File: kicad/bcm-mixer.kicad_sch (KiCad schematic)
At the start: 42 parts, among them J1 AudioJack2_SwitchT, J10 Conn_01x08_Pin, J11 Conn_01x08_Socket, J12 Conn_01x08_Socket, J13 Conn_01x08_Pin, J14 Conn_01x06_Pin, J15 Conn_01x06_Socket, J16 Conn_01x06_Socket, J17 Conn_01x06_Pin, J2 AudioJack2_SwitchT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

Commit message: Updating everything and adding gerbers
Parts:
- removed RV3, RV6: 100kA, Rumblesan_Potentiometer_THT:Potentiometer_TTElectronics_PS45_Dual_Frame, symbol Standard_Parts:R_Potentiometer
- added H1, H2, H3, H4: MountingHole_Pad, Rumblesan_Standard_Parts:MountingHole_3.2mm_M3_DIN965_Pad, symbol Mechanical:MountingHole_Pad
- added RV3, RV6: 100kA, Rumblesan_Potentiometer_THT:Potentiometer_TTElectronics_PS45_Dual_Frame, symbol Rumblesan_Standard_Parts:R_Potentiometer_Dual_Separate
- C19, C20: footprint Capacitor_THT:CP_Radial_D5.0mm_P2.00mm -> Rumblesan_Standard_Parts:CP_Radial_D5.0mm_P2.00mm; symbol Standard_Parts:C_Polarized -> Rumblesan_Standard_Parts:C_Polarized
- R10, R11, R12, R13, R16, R17, R24, R25, R31, R32, R35, R36, R40, R41: symbol Standard_Parts:R -> Rumblesan_Standard_Parts:R
- RV1, RV4: symbol Standard_Parts:R_Potentiometer_Dual_Separate -> Rumblesan_Standard_Parts:R_Potentiometer_Dual_Separate
- RV10, RV2, RV5, RV9: symbol Standard_Parts:R_Potentiometer -> Rumblesan_Standard_Parts:R_Potentiometer
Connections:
- net CHAN1_LEVEL_CENTER_CTRL: now also RV3.2
- net CHAN1_LEVEL_CW_CTRL: now also RV3.3
- net CHAN1_PAN_CCW_MAIN: now also R11.2, R13.1; no longer R11.1, R13.2
- net CHAN1_PAN_CW_MAIN: now also R10.2, R12.1; no longer R10.1, R12.2
- net CHAN2_LEVEL_CENTER_CTRL: now also RV6.2
- net CHAN2_LEVEL_CW_CTRL: now also RV6.3
- net CHAN2_PAN_CCW_MAIN: now also R17.2, R24.1; no longer R17.1, R24.2
- net CHAN2_PAN_CW_MAIN: now also R16.2, R25.1; no longer R16.1, R25.2
- net GND: now also H1.1, H2.1, H3.1, H4.1, RV3.1, RV3.6, RV6.1, RV6.6
- net L_OUT_MAIN: now also R40.2; no longer R40.1
- net MAIN_BUS_L: now also R12.2, R25.2, R31.2, R35.2; no longer R12.1, R25.1, R31.1, R35.1
- net MAIN_BUS_R: now also R13.2, R24.2, R32.2, R36.1; no longer R13.1, R24.1, R32.1, R36.2
- net Main Channel/L_OUT: now also R40.1; no longer R40.2
- net Main Channel/R_OUT: now also R41.1; no longer R41.2
- net Mono Channel 1/OUTPUT: now also R10.1, R11.1; no longer R10.2, R11.2
- net Mono Channel 2/OUTPUT: now also R16.1, R17.1; no longer R16.2, R17.2
- net R_OUT_MAIN: now also R41.2; no longer R41.1
- net at J14.3 (Pin_3): now also R32.1; no longer R32.2
- net at J14.5 (Pin_5): now also R31.1; no longer R31.2
- net at J8.7 (Pin_7), J8.8 (Pin_8): now also R36.2; no longer R36.1
- net at J8.3 (Pin_3), J8.4 (Pin_4): now also R35.1; no longer R35.2
- no-connect marks 4 -> 8

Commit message: Updating power header symbol
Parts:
- J6: footprint Rumblesan_Eurorack_Power:Eurorack_PowerHeader_2x05_P2.54mm_Shrouded -> Rumblesan_Eurorack_Power:Eurorack_Power_IDC-Header_2x05_P2.54mm_Vertical

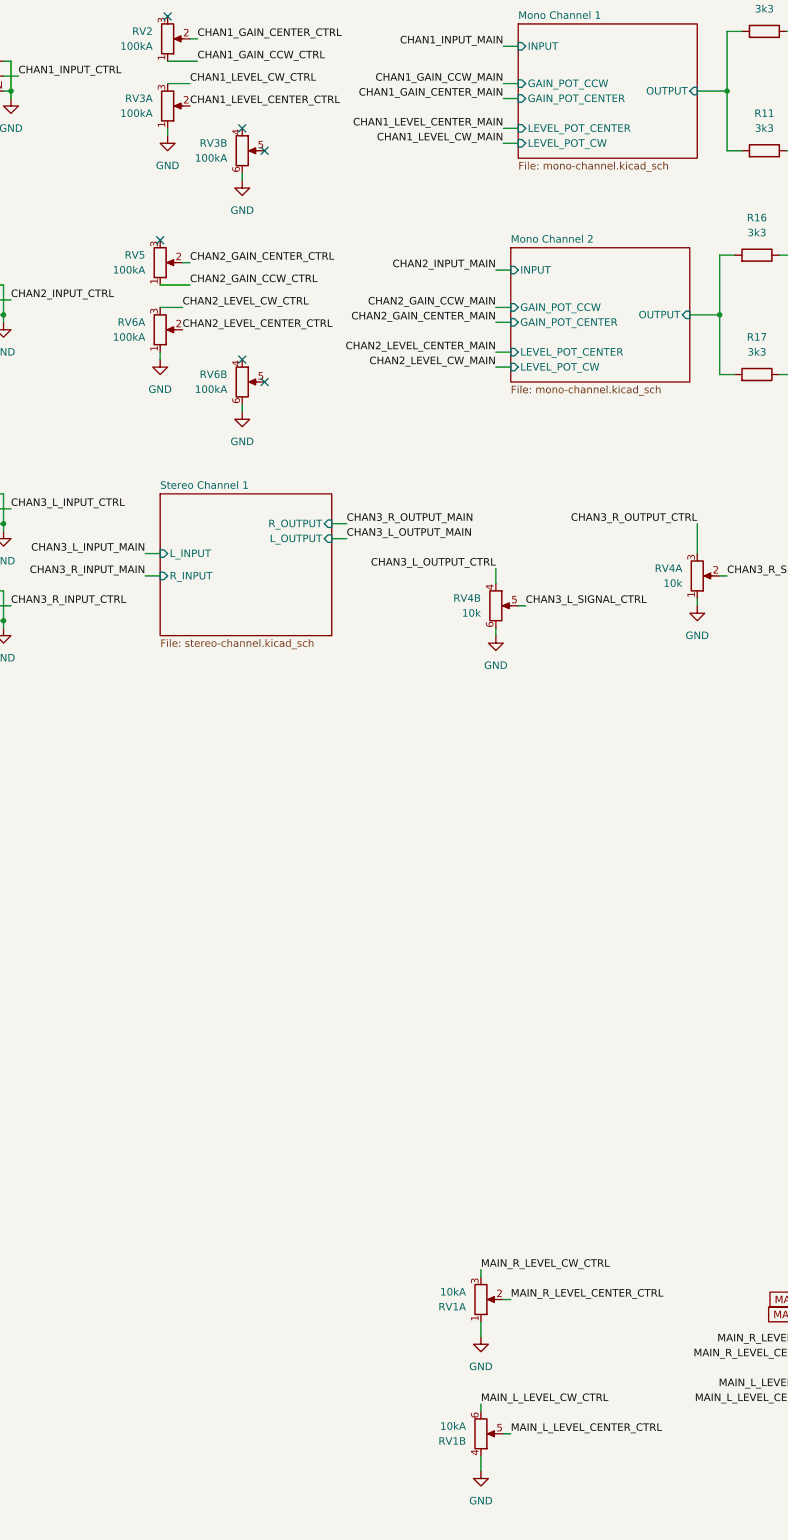
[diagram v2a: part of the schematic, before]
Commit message: Update slide pot values based on what's actually available
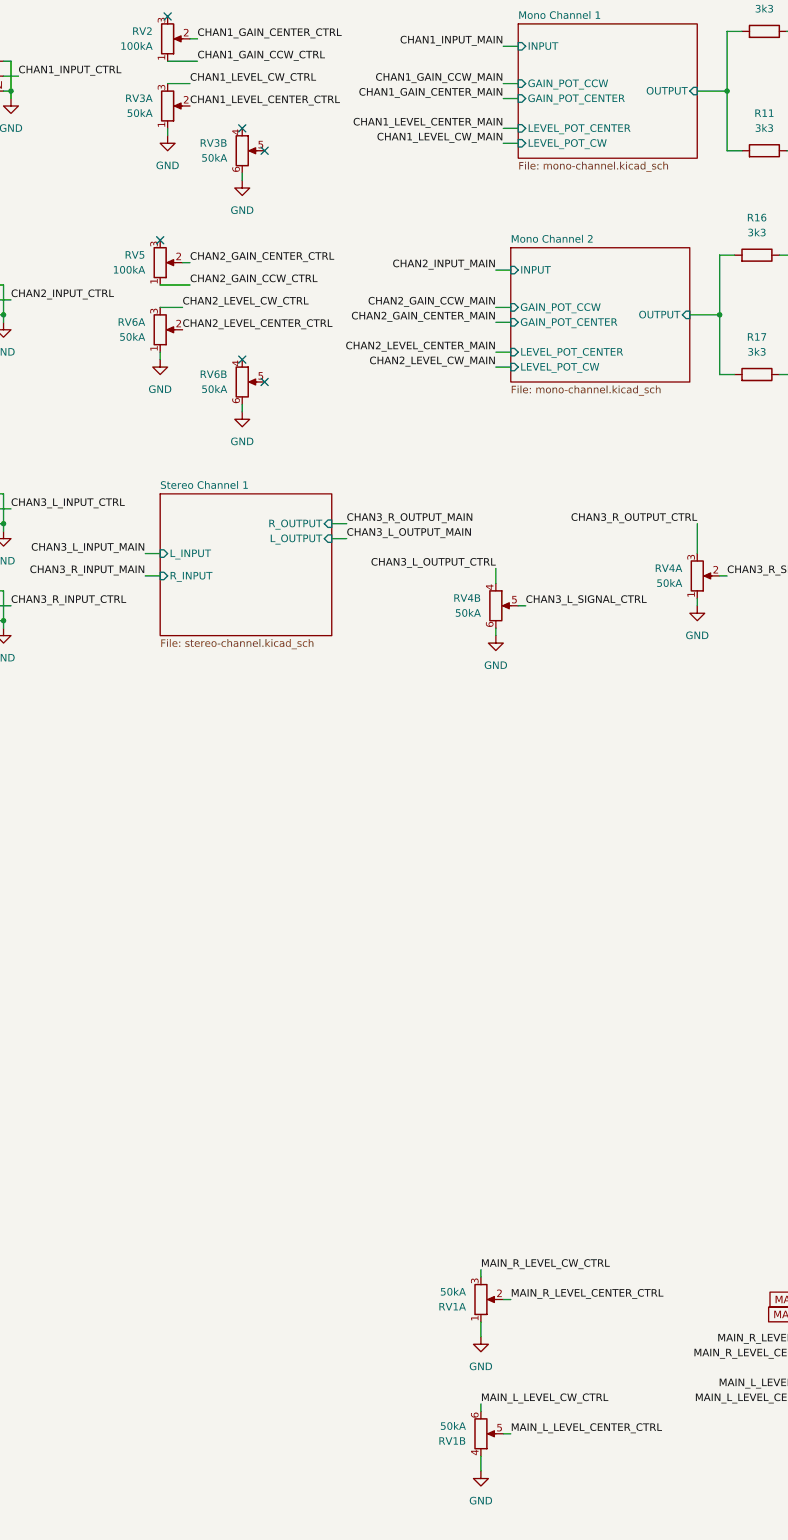
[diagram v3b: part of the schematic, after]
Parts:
- RV1: value 10kA -> 50kA
- RV3, RV6: value 100kA -> 50kA
- RV4: value 10k -> 50kA
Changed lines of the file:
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@@
 			)
 		)
-		(property "Value" "10k"
+		(property "Value" "50kA"
 			(at 147.32 118.1099 0)
 			(effects
@@
 			)
 		)
-		(property "Value" "10kA"
+		(property "Value" "50kA"
 			(at 110.49 238.7601 0)
 			(effects
@@
 			)
 		)
-		(property "Value" "100kA"
+		(property "Value" "50kA"
 			(at 69.85 45.7199 0)
 			(effects
@@
 			)
 		)
-		(property "Value" "10kA"
+		(property "Value" "50kA"
 			(at 110.49 261.6201 0)
 			(effects
@@
 			)
 		)
-		(property "Value" "100kA"
+		(property "Value" "50kA"
 			(at 55.88 76.1999 0)
 			(effects
@@
 			)
 		)
-		(property "Value" "100kA"
+		(property "Value" "50kA"
 			(at 57.15 38.0999 0)
 			(effects
@@
 			)
 		)
-		(property "Value" "100kA"
+		(property "Value" "50kA"
 			(at 69.85 85.0899 0)
 			(effects
@@
 			)
 		)
-		(property "Value" "10k"
+		(property "Value" "50kA"
 			(at 113.03 123.1899 0)
 			(effects

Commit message: Updating for revision 2
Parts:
- added H5: MountingHole, MountingHole:MountingHole_3.2mm_M3_DIN965, symbol Mechanical:MountingHole
- R10, R11, R16, R17: value 3k3 -> 22k
- R12, R13, R24, R25: value 12k -> 22k
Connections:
- net CHAN1_LEVEL_CW_CTRL: now also RV3.1; no longer RV3.3
- net CHAN2_LEVEL_CW_CTRL: now also RV6.1; no longer RV6.3
- net CHAN3_R_OUTPUT_CTRL: now also RV4.1; no longer RV4.3
- net GND: now also RV1.3, RV1.6, RV3.3, RV4.3, RV6.3; no longer RV1.1, RV1.4, RV3.1, RV4.1, RV6.1
- net MAIN_L_LEVEL_CW_CTRL: now also RV1.4; no longer RV1.6
- net MAIN_R_LEVEL_CW_CTRL: now also RV1.1; no longer RV1.3
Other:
- moved on the sheet: C19, C20, D1, D2, J1, J14, J15, J16, J17, J2, J6, J8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
